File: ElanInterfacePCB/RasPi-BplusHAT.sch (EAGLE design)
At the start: 41 parts, among them K1 PIN20X2, Q1 220mA/50V/3.5Ω, Q10 1.1A/60V/600mΩ, Q12 1.1A/60V/600mΩ, Q13 220mA/50V/3.5Ω, Q2 1.1A/60V/600mΩ, Q3 220mA/50V/3.5Ω, Q4 1.1A/60V/600mΩ, Q5 220mA/50V/3.5Ω, Q6 1.1A/60V/600mΩ, Q7 220mA/50V/3.5Ω, Q8 1.1A/60V/600mΩ, Q9 220mA/50V/3.5Ω, U2 MAX481CUA+

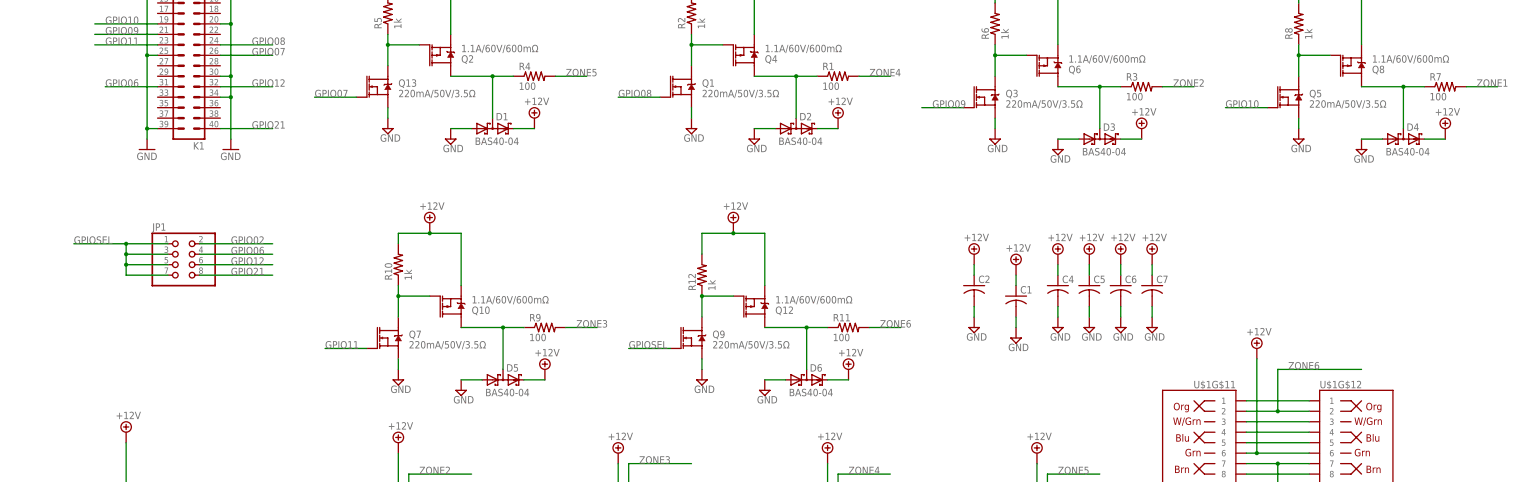
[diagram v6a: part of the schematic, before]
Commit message: Reworking Board smaller
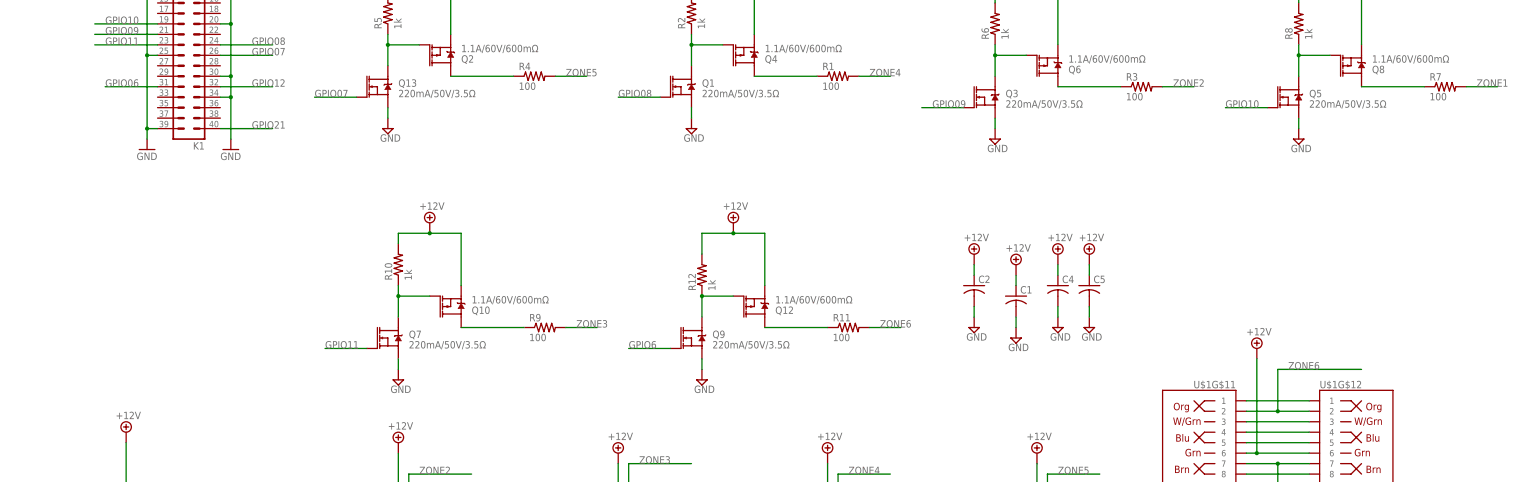
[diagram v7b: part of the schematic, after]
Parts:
- removed C6, C7: (no value), rcl:C-USC0805
- removed D1, D2, D3, D4, D5, D6: BAS40-04, diode:BAS40-04
- removed JP1: (no value), pinhead:PINHD-2X4
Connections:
- removed net GPIOSEL: JP1.1, JP1.3, JP1.5, JP1.7, Q9.G
- new net GPIO6: Q9.G
- net +12V: no longer C6.1, C7.1, D1.C2, D2.C2, D3.C2, D4.C2, D5.C2, D6.C2
- net GND: no longer C6.2, C7.2, D1.A1, D2.A1, D3.A1, D4.A1, D5.A1, D6.A1
- net GPIO02: no longer JP1.2
- net GPIO06: no longer JP1.4
- net GPIO12: no longer JP1.6
- net GPIO21: no longer JP1.8
- net N$10: no longer D5.C1A2
- net N$12: no longer D6.C1A2
- net N$2: no longer D2.C1A2
- net N$5: no longer D1.C1A2
- net N$6: no longer D3.C1A2
- net N$8: no longer D4.C1A2
